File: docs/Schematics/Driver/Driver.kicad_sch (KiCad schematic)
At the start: 0 parts

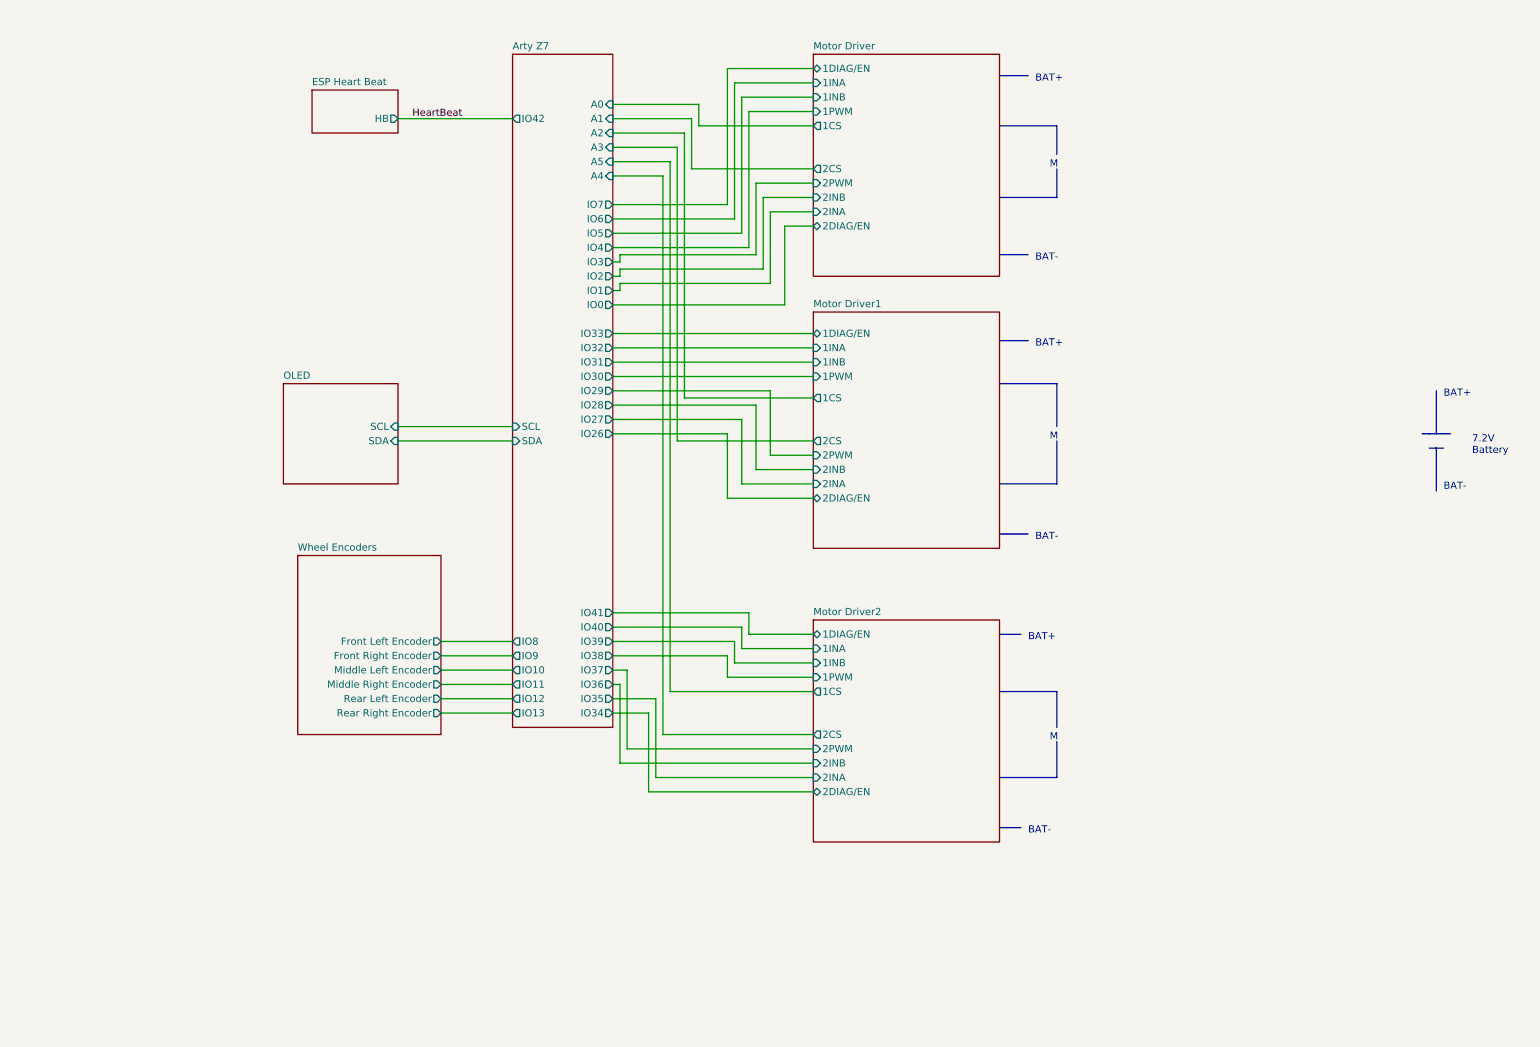
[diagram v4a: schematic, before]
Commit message: Added caps and changed the connection from the motor sensors to plints
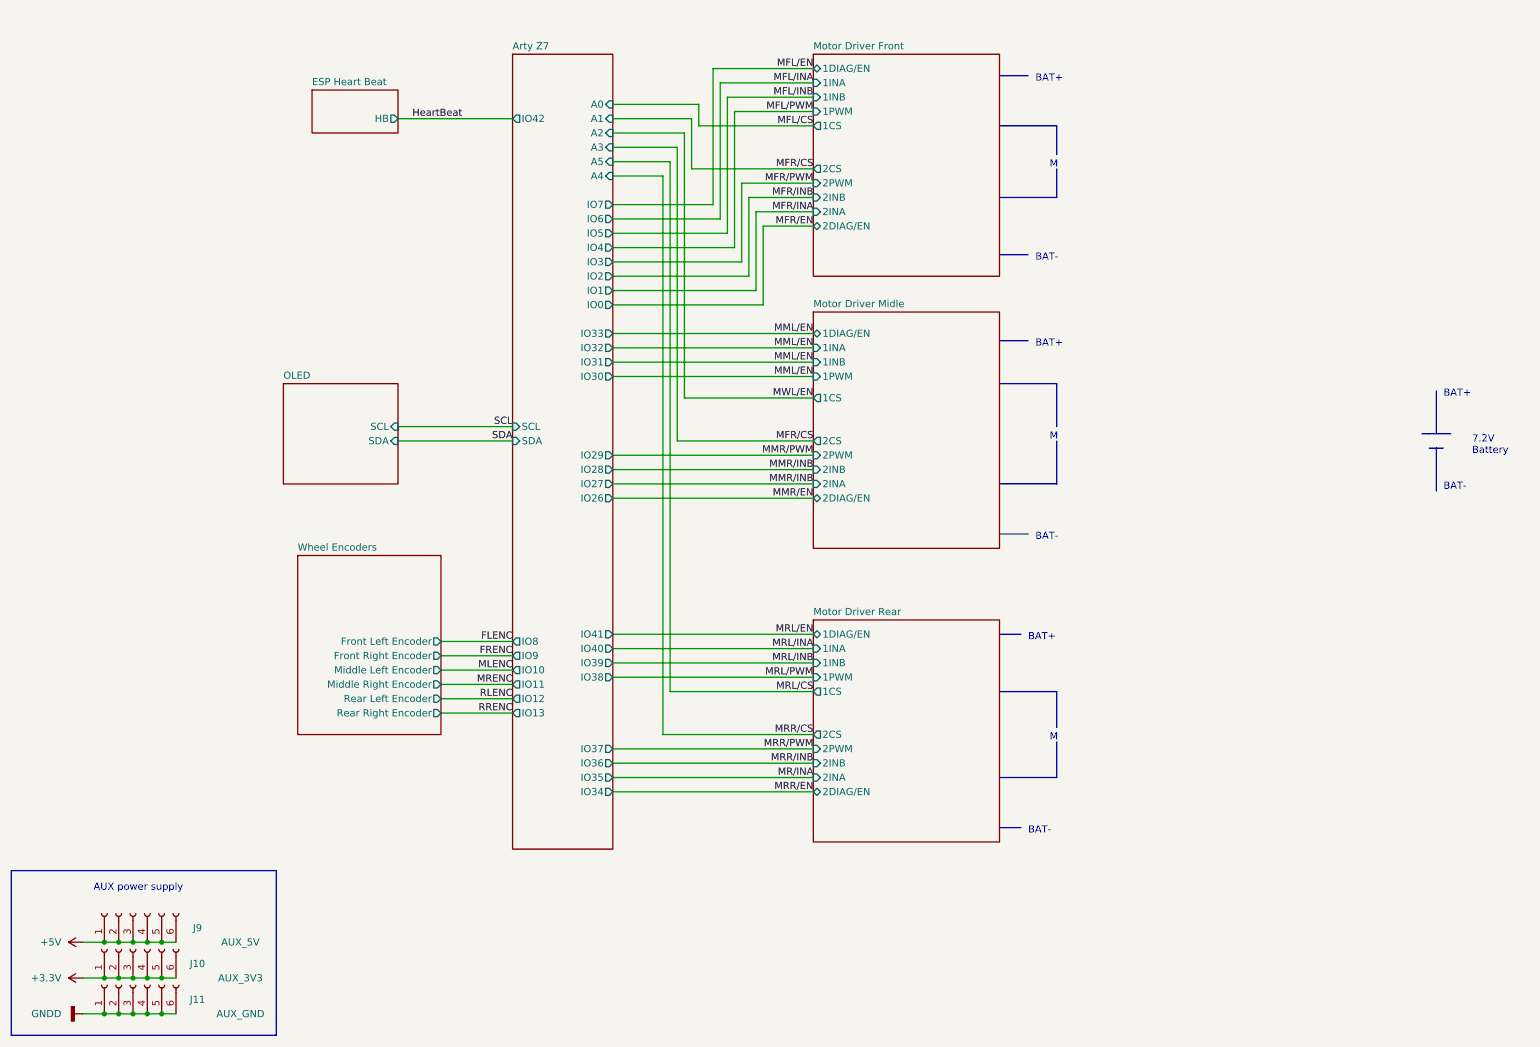
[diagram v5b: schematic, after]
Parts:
- added J10: AUX_3V3, Connector_PinSocket_2.54mm:PinSocket_1x06_P2.54mm_Vertical, symbol Connector:Conn_01x06_Female
- added J11: AUX_GND, Connector_PinSocket_2.54mm:PinSocket_1x06_P2.54mm_Vertical, symbol Connector:Conn_01x06_Female
- added J9: AUX_5V, Connector_PinSocket_2.54mm:PinSocket_1x06_P2.54mm_Vertical, symbol Connector:Conn_01x06_Female
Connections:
- new net +3.3V: J10.1 (Pin_1), J10.2 (Pin_2), J10.3 (Pin_3), J10.4 (Pin_4), J10.5 (Pin_5), J10.6 (Pin_6)
- new net +5V: J9.1 (Pin_1), J9.2 (Pin_2), J9.3 (Pin_3), J9.4 (Pin_4), J9.5 (Pin_5), J9.6 (Pin_6)
- new net GNDD: J11.1 (Pin_1), J11.2 (Pin_2), J11.3 (Pin_3), J11.4 (Pin_4), J11.5 (Pin_5), J11.6 (Pin_6)
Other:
- sheet Motor Driver renamed Motor Driver Front
- sheet Motor Driver1 renamed Motor Driver Midle
- sheet Motor Driver2 renamed Motor Driver Rear
- note added: "AUX power supply"

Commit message: Started routing the pcb.
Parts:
- added H? (x4): MountingHole, MountingHole:MountingHole_3.2mm_M3, symbol Mechanical:MountingHole

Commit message: Changed a few nets to make the routing posible
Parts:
- gave numbers to parts that had none: 4
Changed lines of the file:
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@@
   (symbol (lib_id "Mechanical:MountingHole") (at 95.25 184.15 0) (unit 1)
     (in_bom yes) (on_board yes) (fields_autoplaced)
-    (property "Reference" "H?" (id 0) (at 97.79 182.8799 0)
+    (property "Reference" "H3" (id 0) (at 97.79 182.8799 0)
       (effects (font (size 1.27 1.27)) (justify left))
     )
@@
   (symbol (lib_id "Mechanical:MountingHole") (at 73.66 190.5 0) (unit 1)
     (in_bom yes) (on_board yes) (fields_autoplaced)
-    (property "Reference" "H?" (id 0) (at 76.2 189.2299 0)
+    (property "Reference" "H2" (id 0) (at 76.2 189.2299 0)
       (effects (font (size 1.27 1.27)) (justify left))
     )
@@
   (symbol (lib_id "Mechanical:MountingHole") (at 95.25 190.5 0) (unit 1)
     (in_bom yes) (on_board yes) (fields_autoplaced)
-    (property "Reference" "H?" (id 0) (at 97.79 189.2299 0)
+    (property "Reference" "H4" (id 0) (at 97.79 189.2299 0)
       (effects (font (size 1.27 1.27)) (justify left))
     )
@@
   (symbol (lib_id "Mechanical:MountingHole") (at 73.66 184.15 0) (unit 1)
     (in_bom yes) (on_board yes) (fields_autoplaced)
-    (property "Reference" "H?" (id 0) (at 76.2 182.8799 0)
+    (property "Reference" "H1" (id 0) (at 76.2 182.8799 0)
       (effects (font (size 1.27 1.27)) (justify left))
     )
@@
       (effects (font (size 1.27 1.27)) (justify right))
     )
-    (pin "A2" input (at 121.92 35.56 0)
-      (effects (font (size 1.27 1.27)) (justify right))
-    )
-    (pin "A3" input (at 121.92 38.1 0)
+    (pin "A2" input (at 121.92 38.1 0)
+      (effects (font (size 1.27 1.27)) (justify right))
+    )
+    (pin "A3" input (at 121.92 35.56 0)
       (effects (font (size 1.27 1.27)) (justify right))
     )
@@
       (effects (font (size 1.27 1.27)) (justify right))
     )
-    (pin "IO28" output (at 121.92 95.25 0)
-      (effects (font (size 1.27 1.27)) (justify right))
-    )
-    (pin "IO27" output (at 121.92 97.79 0)
-      (effects (font (size 1.27 1.27)) (justify right))
-    )
-    (pin "IO29" output (at 121.92 92.71 0)
-      (effects (font (size 1.27 1.27)) (justify right))
-    )
-    (pin "IO26" output (at 121.92 100.33 0)
-      (effects (font (size 1.27 1.27)) (justify right))
-    )
-    (pin "IO33" output (at 121.92 71.12 0)
-      (effects (font (size 1.27 1.27)) (justify right))
-    )
-    (pin "IO30" output (at 121.92 78.74 0)
-      (effects (font (size 1.27 1.27)) (justify right))
-    )
-    (pin "IO32" output (at 121.92 73.66 0)
-      (effects (font (size 1.27 1.27)) (justify right))
-    )
-    (pin "IO31" output (at 121.92 76.2 0)
+    (pin "IO28" output (at 121.92 76.2 0)
+      (effects (font (size 1.27 1.27)) (justify right))
+    )
+    (pin "IO27" output (at 121.92 73.66 0)
+      (effects (font (size 1.27 1.27)) (justify right))
+    )
+    (pin "IO29" output (at 121.92 78.74 0)
+      (effects (font (size 1.27 1.27)) (justify right))
+    )
+    (pin "IO26" output (at 121.92 71.12 0)
+      (effects (font (size 1.27 1.27)) (justify right))
+    )
+    (pin "IO33" output (at 121.92 100.33 0)
+      (effects (font (size 1.27 1.27)) (justify right))
+    )
+    (pin "IO30" output (at 121.92 92.71 0)
+      (effects (font (size 1.27 1.27)) (justify right))
+    )
+    (pin "IO32" output (at 121.92 97.79 0)
+      (effects (font (size 1.27 1.27)) (justify right))
+    )
+    (pin "IO31" output (at 121.92 95.25 0)
       (effects (font (size 1.27 1.27)) (justify right))
     )
@@
       (effects (font (size 1.27 1.27)) (justify left))
     )
-    (pin "IO41" output (at 121.92 124.46 0)
-      (effects (font (size 1.27 1.27)) (justify right))
-    )
-    (pin "IO40" output (at 121.92 127 0)
-      (effects (font (size 1.27 1.27)) (justify right))
-    )
-    (pin "IO39" output (at 121.92 129.54 0)
-      (effects (font (size 1.27 1.27)) (justify right))
-    )
-    (pin "IO38" output (at 121.92 132.08 0)
-      (effects (font (size 1.27 1.27)) (justify right))
-    )
-    (pin "IO37" output (at 121.92 144.78 0)
+    (pin "IO41" output (at 121.92 152.4 0)
+      (effects (font (size 1.27 1.27)) (justify right))
+    )
+    (pin "IO40" output (at 121.92 149.86 0)
+      (effects (font (size 1.27 1.27)) (justify right))
+    )
+    (pin "IO39" output (at 121.92 147.32 0)
+      (effects (font (size 1.27 1.27)) (justify right))
+    )
+    (pin "IO38" output (at 121.92 144.78 0)
+      (effects (font (size 1.27 1.27)) (justify right))
+    )
+    (pin "IO37" output (at 121.92 132.08 0)
       (effects (font (size 1.27 1.27)) (justify right))
     )
@@
       (effects (font (size 1.27 1.27)) (justify left))
     )
-    (pin "IO36" output (at 121.92 147.32 0)
+    (pin "IO36" output (at 121.92 129.54 0)
       (effects (font (size 1.27 1.27)) (justify right))
     )
@@
       (effects (font (size 1.27 1.27)) (justify left))
     )
-    (pin "IO35" output (at 121.92 149.86 0)
-      (effects (font (size 1.27 1.27)) (justify right))
-    )
-    (pin "IO34" output (at 121.92 152.4 0)
+    (pin "IO35" output (at 121.92 127 0)
+      (effects (font (size 1.27 1.27)) (justify right))
+    )
+    (pin "IO34" output (at 121.92 124.46 0)
       (effects (font (size 1.27 1.27)) (justify right))
     )
@@
       (reference "C18") (unit 1) (value "C_Polarized") (footprint "Capacitor_SMD:C_0805_2012Metric_Pad1.18x1.45mm_HandSolder")
     )
+    (path "/963b2533-799e-4061-9fee-caedf26cfde0"
+      (reference "H1") (unit 1) (value "MountingHole") (footprint "MountingHole:MountingHole_3.2mm_M3")
+    )
+    (path "/4d9bbce4-8ea7-4ba0-bfdb-82edc827e571"
+      (reference "H2") (unit 1) (value "MountingHole") (footprint "MountingHole:MountingHole_3.2mm_M3")
+    )
     (path "/134c2386-5a7e-4f26-8b29-b24cb965e763"
-      (reference "H?") (unit 1) (value "MountingHole") (footprint "MountingHole:MountingHole_3.2mm_M3")
-    )
-    (path "/4d9bbce4-8ea7-4ba0-bfdb-82edc827e571"
-      (reference "H?") (unit 1) (value "MountingHole") (footprint "MountingHole:MountingHole_3.2mm_M3")
+      (reference "H3") (unit 1) (value "MountingHole") (footprint "MountingHole:MountingHole_3.2mm_M3")
     )
     (path "/63310b66-1663-4cf0-99fb-8eb0d0031938"
-      (reference "H?") (unit 1) (value "MountingHole") (footprint "MountingHole:MountingHole_3.2mm_M3")
-    )
-    (path "/963b2533-799e-4061-9fee-caedf26cfde0"
-      (reference "H?") (unit 1) (value "MountingHole") (footprint "MountingHole:MountingHole_3.2mm_M3")
+      (reference "H4") (unit 1) (value "MountingHole") (footprint "MountingHole:MountingHole_3.2mm_M3")
     )
     (path "/73a52613-ecb4-4016-9dfa-6685718f0c6b/a012799e-efb3-464d-b95e-963a96eb0253"
